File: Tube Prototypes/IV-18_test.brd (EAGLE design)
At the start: 70 x 95 mm, 7 parts

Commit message: update IV-18 tester
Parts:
- moved R1 31.4 mm to (8.99, 49.5), turned to 270 degrees
- moved U$1 9.52 mm to (33.2, 28.5), flipped to the top, turned to 270 degrees
- moved DIS1 5.49 mm to (27.8, 52.1), flipped to the bottom, turned to 90 degrees
- moved C2 2.48 mm to (9.59, 23.1), turned to 180 degrees
- moved C1 1.71 mm to (9.75, 29.7), turned to 180 degrees
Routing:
- net GND: track 0.81 -> 103.6 mm, vias 0 -> 1
- net N$16: track 114.3 -> 27.9 mm
- net N$17: track 88.1 -> 32.1 mm
- net N$2: track 93.3 -> 46.2 mm
- net N$11: track 59.5 -> 19.9 mm
- net VCC: track 97.5 -> 64.7 mm, vias 2 -> 0
- net N$10: track 29.1 -> 60.4 mm, vias 0 -> 1
- net N$9: track 43.6 -> 14.9 mm
- net N$12: track 29.7 -> 57.8 mm, vias 0 -> 1
- net N$8: track 23.7 -> 50.9 mm
- net N$13: track 44.3 -> 22.2 mm
- net N$20: track 51.5 -> 29.4 mm, vias 1 -> 2
- net N$1: track 46.4 -> 66.6 mm
- net N$21: track 43.5 -> 23.4 mm
- net N$7: track 12.3 -> 30.9 mm
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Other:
- board text added: "IV-18 TESTER"

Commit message: new
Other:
- board text added: "+40V"
- board text added: "+5V"
- board text added: "Blank"
- board text added: "CLK"
- board text added: "Din"
- board text added: "Dout"
- board text added: "GND"
- board text added: "Load"
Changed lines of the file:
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@@
 <setting verticaltext="up"/>
 </settings>
-<grid distance="1" unitdist="mm" unit="mm" style="lines" multiple="1" display="no" altdistance="0.025" altunitdist="inch" altunit="inch"/>
+<grid distance="0.25" unitdist="mm" unit="mm" style="lines" multiple="1" display="no" altdistance="0.025" altunitdist="inch" altunit="inch"/>
 <layers>
-<layer number="1" name="Top" color="4" fill="1" visible="yes" active="yes"/>
+<layer number="1" name="Top" color="4" fill="1" visible="no" active="yes"/>
 <layer number="2" name="Route2" color="1" fill="3" visible="no" active="no"/>
 <layer number="3" name="Route3" color="4" fill="3" visible="no" active="no"/>
@@
 <text x="7" y="67" size="1.778" layer="1">IV-18 TESTER</text>
 <text x="45" y="67" size="1.778" layer="16" rot="MR0">IV-18 TESTER</text>
+<text x="8.75" y="3.25" size="1.016" layer="25" rot="R90">GND</text>
+<text x="25.5" y="3.25" size="1.016" layer="25" rot="R90">GND</text>
+<text x="13.75" y="3.25" size="1.016" layer="25" rot="R90">+5V</text>
+<text x="11.25" y="3.25" size="1.016" layer="25" rot="R90">+40V</text>
+<text x="28" y="3.25" size="1.016" layer="25" rot="R90">Dout</text>
+<text x="30.5" y="3.25" size="1.016" layer="25" rot="R90">Blank</text>
+<text x="33" y="3.25" size="1.016" layer="25" rot="R90">Load</text>
+<text x="35.75" y="3.25" size="1.016" layer="25" rot="R90">CLK</text>
+<text x="38.5" y="3.25" size="1.016" layer="25" rot="R90">Din</text>
 </plain>
 <attributes>
@@
 </autorouter>
 <elements>
-<element name="U$1" library="iStivi - ICs" package="TSSOP28" value="MAX6921AUI" x="33.17" y="28.51" rot="R270"/>
-<element name="R1" library="iStivi - RCLD" package="0207/10" value="56R" x="8.99" y="49.53" rot="R270"/>
-<element name="JP1" library="iStivi - Header-Connector" package="1X06_LONGPADS" value="" x="25.06" y="9.29"/>
-<element name="C1" library="iStivi - RCLD" package="E2-5" value="10uF" x="9.75" y="29.725" rot="R180"/>
-<element name="C2" library="iStivi - RCLD" package="E2-5" value="100nF" x="9.59" y="23.09" rot="R180"/>
-<element name="JP2" library="iStivi - Header-Connector" package="1X03_LONGPADS" value="" x="8.17" y="9.29"/>
+<element name="U$1" library="iStivi - ICs" package="TSSOP28" value="MAX6921AUI" x="33.17" y="28.51" smashed="yes" rot="R270">
+<attribute name="VALUE" x="27.3488" y="32.9128" size="1.016" layer="27" ratio="10" rot="R270"/>
+</element>
+<element name="R1" library="iStivi - RCLD" package="0207/10" value="56R" x="8.99" y="49.53" smashed="yes" rot="R270">
+<attribute name="VALUE" x="11.605" y="50.7906" size="1.27" layer="27" ratio="10" rot="R270"/>
+</element>
+<element name="JP1" library="iStivi - Header-Connector" package="1X06_LONGPADS" value="" x="25.06" y="9.29" smashed="yes">
+<attribute name="VALUE" x="23.79" y="5.48" size="1.27" layer="27"/>
+</element>
+<element name="C1" library="iStivi - RCLD" package="E2-5" value="10uF" x="9.75" y="29.725" smashed="yes" rot="R180">
+<attribute name="VALUE" x="13.616" y="31.46" size="1.27" layer="27" ratio="10" rot="R270"/>
+</element>
+<element name="C2" library="iStivi - RCLD" package="E2-5" value="100nF" x="9.59" y="23.09" smashed="yes" rot="R180">
+<attribute name="VALUE" x="13.751" y="25.55" size="1.27" layer="27" ratio="10" rot="R270"/>
+</element>
+<element name="JP2" library="iStivi - Header-Connector" package="1X03_LONGPADS" value="" x="8.17" y="9.29" smashed="yes">
+<attribute name="VALUE" x="6.9" y="5.48" size="1.27" layer="27"/>
+</element>
 <element name="DIS1" library="iStivi - Tubes" package="IV-18_SQUARE" value="IV18-SQUARE" x="27.826509375" y="52.10984375" rot="MR90"/>
 </elements>

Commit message: iv-18 board
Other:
- board size 70 x 95 mm -> 50 x 75 mm

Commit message: iv-18
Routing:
- net GND: track 103.6 -> 1.21 mm, vias 1 -> 0
- net N$21: track 23.4 -> 84.3 mm, vias 0 -> 1
- net N$1: track 66.6 -> 29.3 mm, vias 1 -> 0
- net N$14: track 46.2 -> 76.5 mm
- net N$12: track 57.8 -> 83.2 mm
- net N$18: track 46.1 -> 23.7 mm
- net N$3: track 52.9 -> 39.0 mm, vias 0 -> 1
- net N$5: track 29.6 -> 42.5 mm
- net N$9: track 14.9 -> 27.2 mm, vias 0 -> 1
- net N$15: track 38.1 -> 45.7 mm
- net N$17: track 32.1 -> 38.1 mm
- net VCC: track 64.7 -> 59.4 mm, vias 0 -> 1
- net N$19: track 35.0 -> 30.0 mm
- net N$8: track 50.9 -> 55.7 mm, vias 0 -> 2
- net N$2: track 46.2 -> 49.9 mm, vias 1 -> 0
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
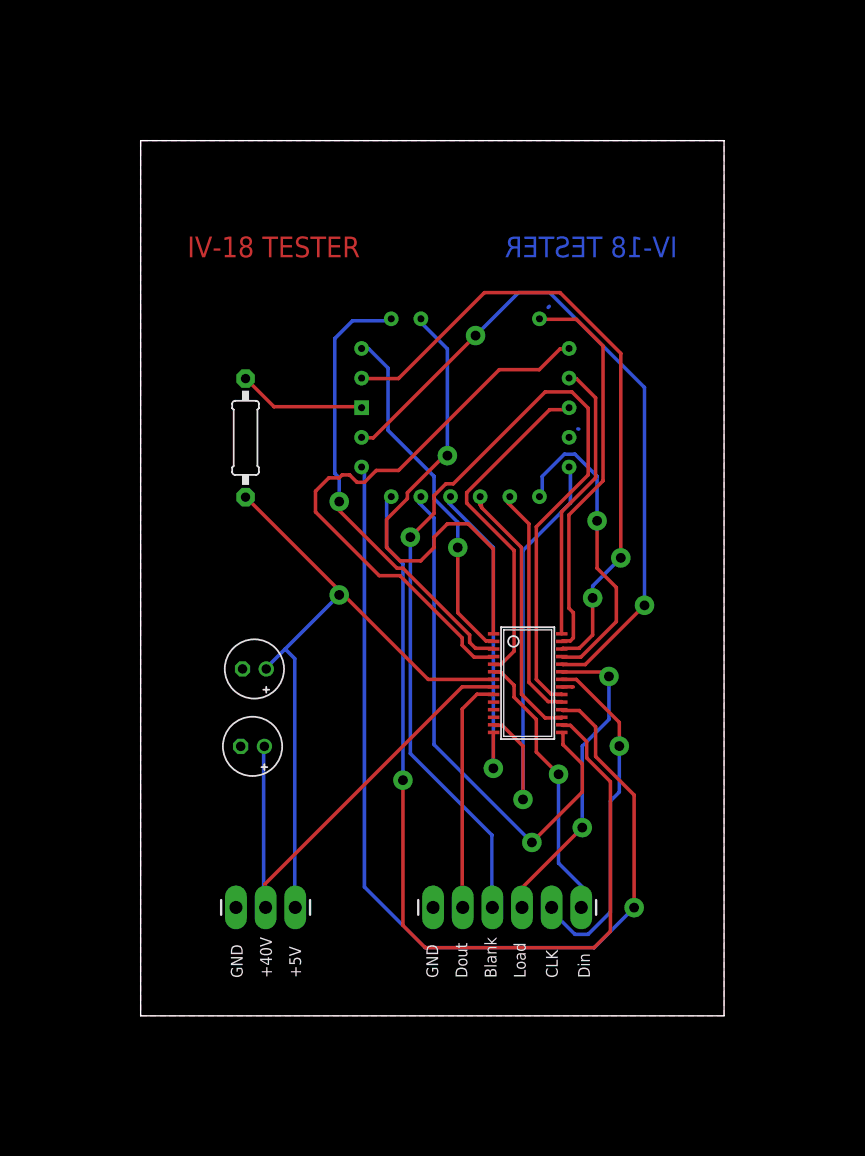
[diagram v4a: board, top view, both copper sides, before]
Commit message: fixed iv-18 boardf
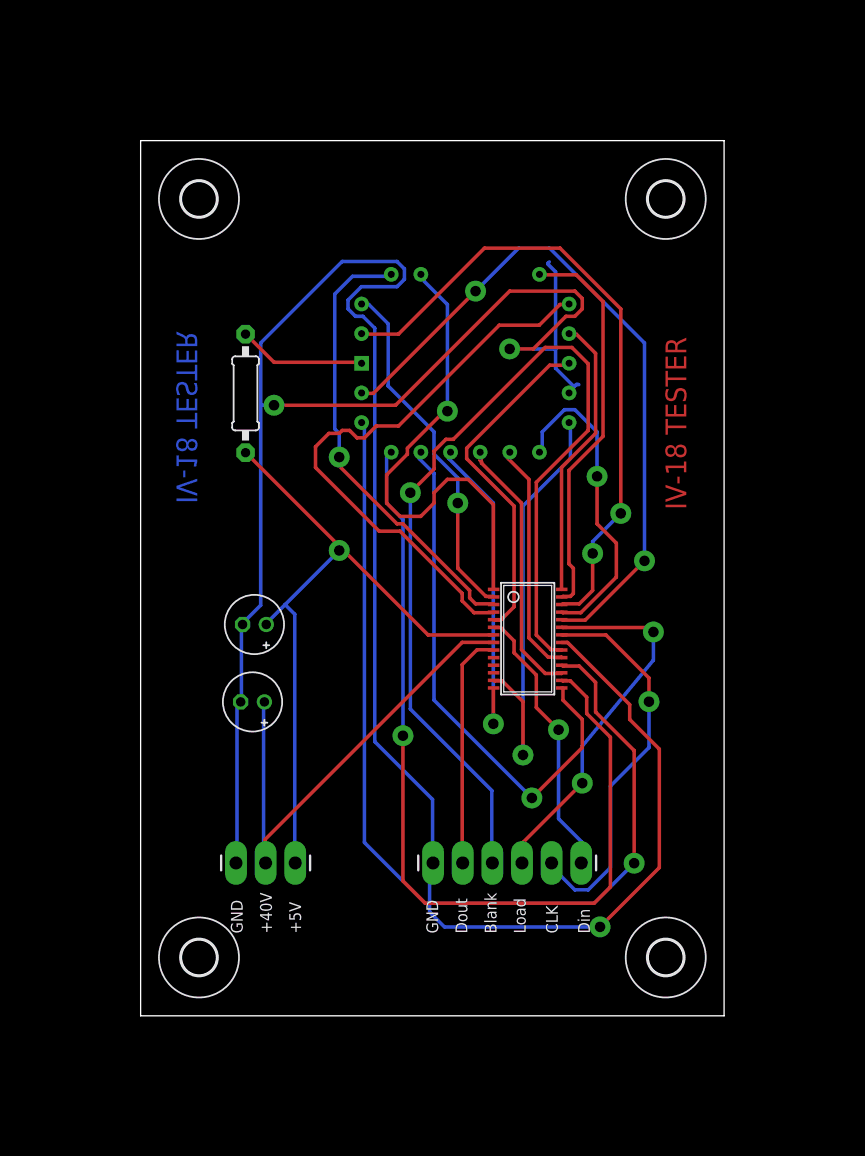
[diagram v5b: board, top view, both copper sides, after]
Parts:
- added U$4, U$5, U$6, U$7: (no value), iStivi - Board-Holes:3,0
- moved R1 3.81 mm to (8.99, 53.3)
- moved JP1 3.81 mm to (25.1, 13.1)
- moved JP2 3.81 mm to (8.17, 13.1)
- moved C2 3.81 mm to (9.59, 26.9)
- moved U$1 3.81 mm to (33.2, 32.3)
- moved C1 3.81 mm to (9.75, 33.5)
- moved DIS1 3.81 mm to (27.8, 55.9)
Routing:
- net GND: track 1.21 -> 225.9 mm, vias 0 -> 3
- net N$20: track 27.1 -> 32.1 mm
- net N$19: track 30.0 -> 33.6 mm
- removed copper zone on layer 1, net GND
- removed copper zone on layer 16, net GND

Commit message: new prototype for dual tube board
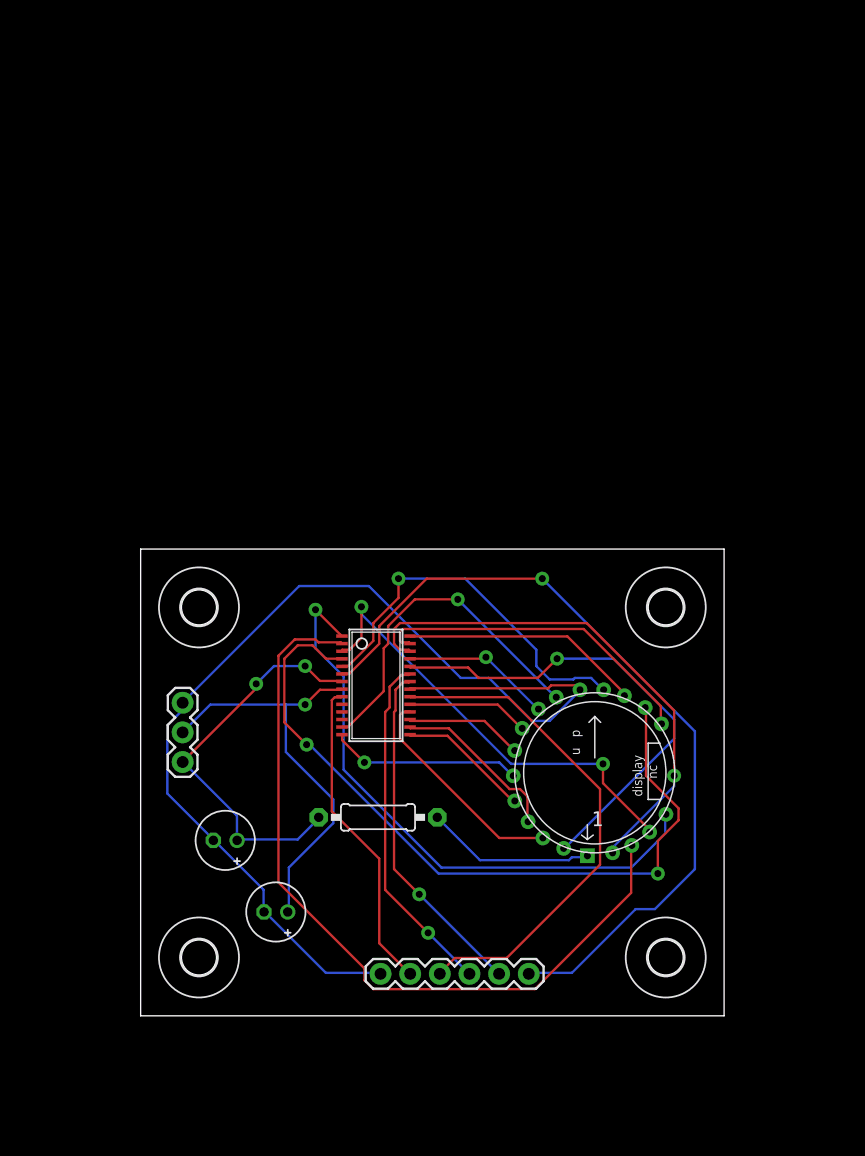
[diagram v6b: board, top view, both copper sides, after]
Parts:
- DIS1: value IV18-SQUARE -> IV18IV-18; device iStivi - Tubes:IV-18_SQUARE -> iStivi - Tubes:IV-18
- JP1: device iStivi - Header-Connector:1X06_LONGPADS -> iStivi - Header-Connector:1X06
- JP2: device iStivi - Header-Connector:1X03_LONGPADS -> iStivi - Header-Connector:1X03
- moved R1 38.1 mm to (20.3, 17.0), turned to 180 degrees
- moved DIS1 36.8 mm to (38.9, 20.8), flipped to the top, turned to 0 degrees
- moved U$4 35.0 mm to (5.00, 35.0)
- moved U$5 35.0 mm to (45.0, 35.0)
- moved C1 18.7 mm to (7.25, 15.0)
- moved C2 18.1 mm to (11.6, 8.90)
- moved JP2 14.5 mm to (3.60, 26.8), turned to 270 degrees
- moved U$1 13.6 mm to (20.2, 28.3)
- moved JP1 10.5 mm to (20.6, 3.60)
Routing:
- net GND: track 225.9 -> 93.1 mm, vias 3 -> 0
- net N$12: track 83.2 -> 18.8 mm, vias 1 -> 0
- net N$14: track 76.5 -> 14.8 mm, vias 1 -> 0
- net N$18: track 23.7 -> 69.8 mm
- net N$21: track 84.3 -> 43.7 mm, vias 1 -> 0
- net N$4: track 30.5 -> 67.7 mm, vias 1 -> 0
- net N$15: track 45.7 -> 11.5 mm, vias 1 -> 0
- net VCC: track 59.4 -> 34.3 mm, vias 1 -> 2
- net N$10: track 60.6 -> 40.9 mm, vias 2 -> 1
- net N$2: track 49.9 -> 64.8 mm, vias 0 -> 2
- net N$9: track 27.2 -> 12.9 mm
- net N$13: track 22.9 -> 10.1 mm
- net N$16: track 28.0 -> 16.4 mm
- net N$8: track 55.7 -> 44.6 mm, vias 2 -> 1
- net N$11: track 20.2 -> 10.5 mm
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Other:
- board size 50 x 75 mm -> 50 x 40 mm
- board text added: "1"
- board text added: "40V"
- board text added: "5V"
- board text added: "TOP"
- board text added: "disp."
- board text added: "nc"
- board text removed: "+40V"
- board text removed: "+5V"
- board text removed: "IV-18 TESTER"
